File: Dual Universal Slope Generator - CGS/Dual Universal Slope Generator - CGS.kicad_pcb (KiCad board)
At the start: 2 copper layers, 115.3 x 110 mm, 146 parts, among them J1 CV_IN_A, J10 TRIG_IN_B, J11 IN_B, J12 1V/OCT_B, J13 DC_OUT_B, J14 AC_COUPLED_OUT_B, J15 END_OUT_B, J16 BIPOLAR_OUT_B, J17 CV_POT_A, J18 FALL_POT_A, J19 RISE_POT_A, J2 TRIG_IN_A, J20 SW_RISE_A, J21 SW_FALL_A, J22 CV_POT_2_B, J23 FALL_POT_B, J24 RISE_POT_B, J25 SW_RISE_B, J26 SW_FALL_B, J3 IN_A, J4 1V/OCT_A, J5 DC_OUT_A, J6 AC_COUPLED_OUT_A, J7 END_OUT_A, J8 BIPOLAR_OUT_A, J9 CV_IN_B, Q1 2N3904, Q10 2N3906, Q11 2N3904, Q2 2N3906, Q3 2N3906, Q4 2N3906, Q5 2N3904, Q7 2N3904, Q8 2N3906, Q9 2N3906, U1 LF353, U2 TL072, U3 LM3900, U4 LF353, U5 TL072, U6 LM3900

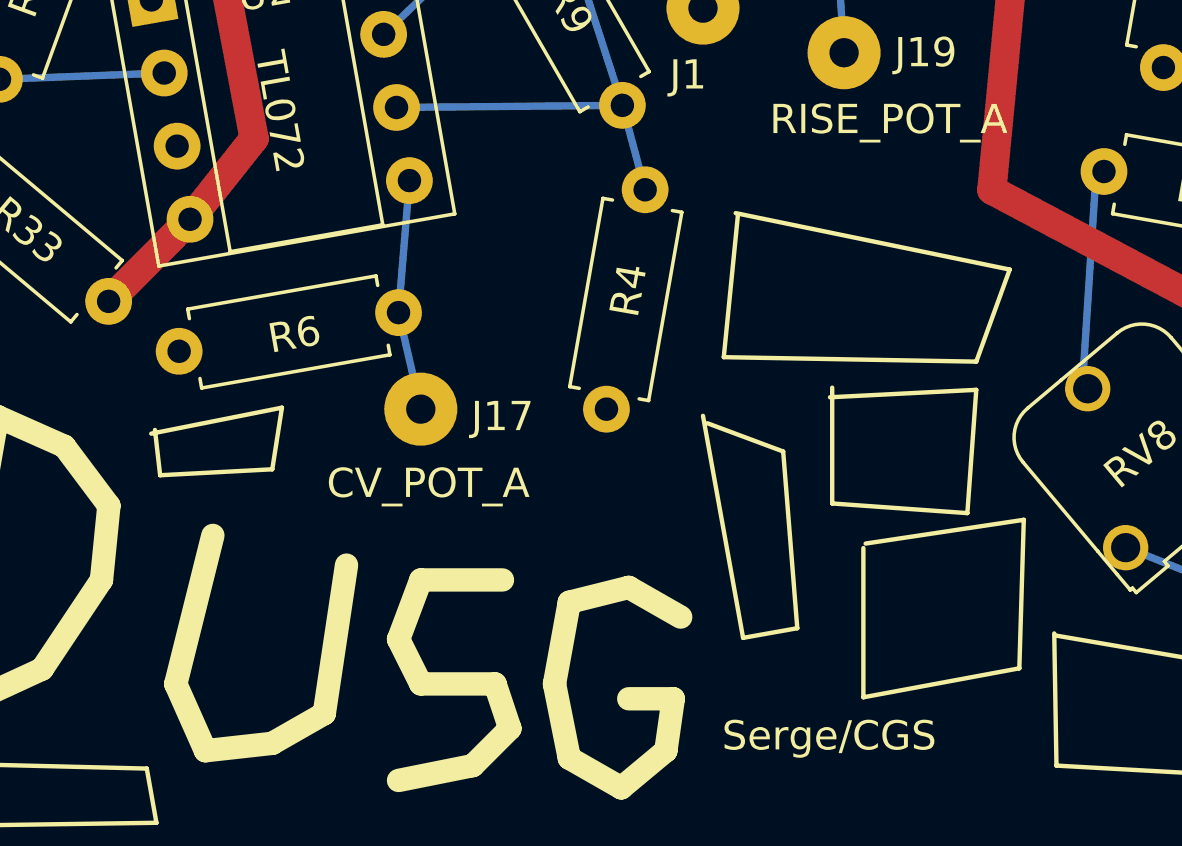
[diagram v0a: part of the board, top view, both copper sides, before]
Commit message: added power connectors to DUSG
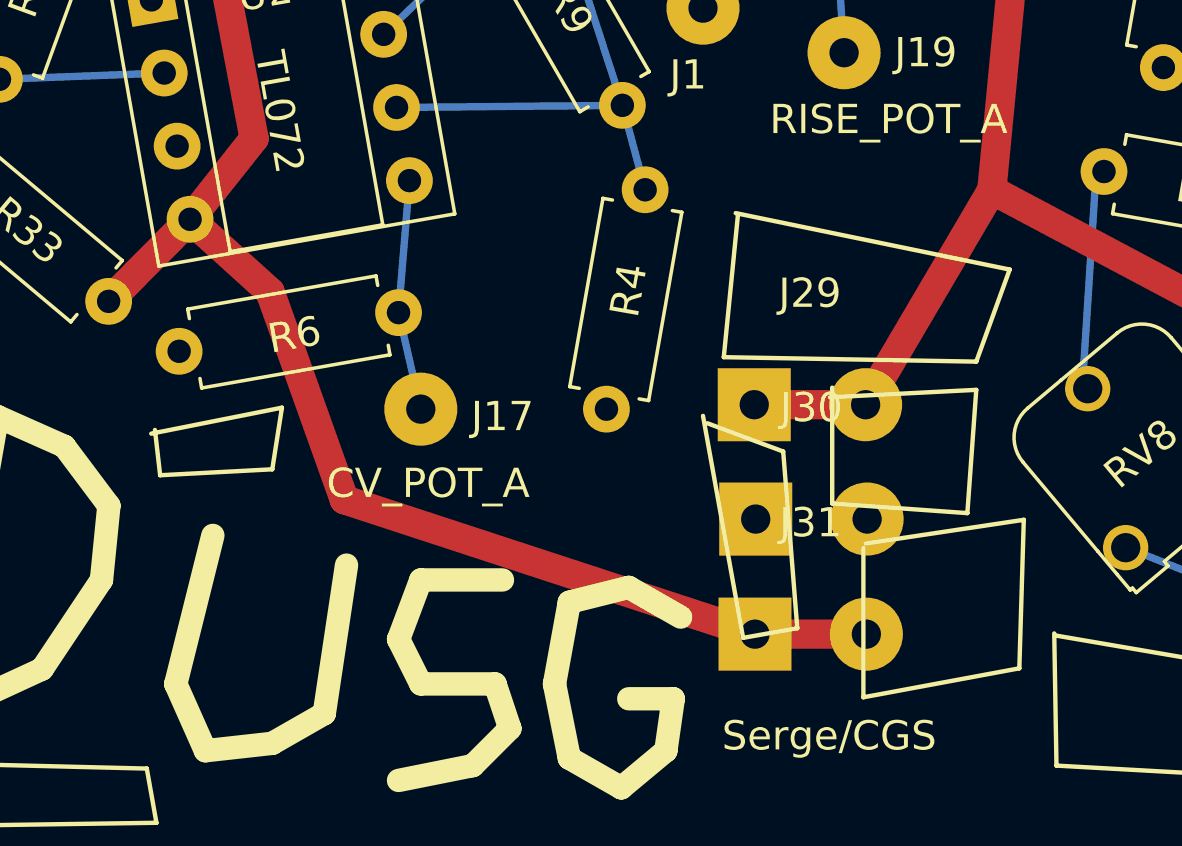
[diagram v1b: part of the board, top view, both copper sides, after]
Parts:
- added J29: +12V_Conn, Connector_Wire:SolderWirePad_1x02_P3.81mm_Drill1mm, F.Cu at (51.8, 106.5)
- added J30: GND_Conn, Connector_Wire:SolderWirePad_1x02_P3.81mm_Drill1mm, F.Cu at (51.8, 110.4)
- added J31: -12V_Conn, Connector_Wire:SolderWirePad_1x02_P3.81mm_Drill1mm, F.Cu at (51.8, 114.4)
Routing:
- net -12V: track 227.1 -> 256.9 mm
- net +12V: track 285.9 -> 298.2 mm
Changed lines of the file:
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@@
     (thickness 1.6)
     (drawings 1897)
-    (tracks 439)
+    (tracks 445)
     (zones 0)
-    (modules 146)
+    (modules 149)
     (nets 92)
   )
@@
     (44 Edge.Cuts user)
     (45 Margin user)
-    (46 B.CrtYd user hide)
-    (47 F.CrtYd user hide)
+    (46 B.CrtYd user)
+    (47 F.CrtYd user)
     (48 B.Fab user hide)
     (49 F.Fab user hide)
@@
     (add_net "Net-(U6-Pad5)")
   )
+  (module Connector_Wire:SolderWirePad_1x02_P3.81mm_Drill1mm (layer F.Cu)
+    (at 51.816 114.3762)
+    (descr "Wire solder connection")
+    (tags connector)
+    (attr virtual)
+    (fp_text reference J31 (at 1.905 -3.81) (layer F.SilkS)
+      (effects (font (size 1 1) (thickness 0.15)))
+    )
+    (fp_text value -12V_Conn (at 1.905 3.81) (layer F.Fab)
+      (effects (font (size 1 1) (thickness 0.15)))
+    )
+    (fp_line (start 5.56 1.75) (end -1.74 1.75) (layer F.CrtYd) (width 0.05))
+    (fp_line (start 5.56 1.75) (end 5.56 -1.75) (layer F.CrtYd) (width 0.05))
+    (fp_line (start -1.74 -1.75) (end -1.74 1.75) (layer F.CrtYd) (width 0.05))
+    (fp_line (start -1.74 -1.75) (end 5.56 -1.75) (layer F.CrtYd) (width 0.05))
+    (fp_text user %R (at 1.905 0) (layer F.Fab)
+      (effects (font (size 1 1) (thickness 0.15)))
+    )
+    (pad 2 thru_hole circle (at 3.81 0) (size 2.49936 2.49936) (drill 1.00076) (layers *.Cu *.Mask)
+      (net 70 -12V))
+    (pad 1 thru_hole rect (at 0 0) (size 2.49936 2.49936) (drill 1.00076) (layers *.Cu *.Mask)
+      (net 70 -12V))
+  )
+  (module Connector_Wire:SolderWirePad_1x02_P3.81mm_Drill1mm (layer F.Cu)
+    (at 51.8414 110.4392)
+    (descr "Wire solder connection")
+    (tags connector)
+    (attr virtual)
+    (fp_text reference J30 (at 1.905 -3.81) (layer F.SilkS)
+      (effects (font (size 1 1) (thickness 0.15)))
+    )
+    (fp_text value GND_Conn (at 1.905 3.81) (layer F.Fab)
+      (effects (font (size 1 1) (thickness 0.15)))
+    )
+    (fp_line (start 5.56 1.75) (end -1.74 1.75) (layer F.CrtYd) (width 0.05))
+    (fp_line (start 5.56 1.75) (end 5.56 -1.75) (layer F.CrtYd) (width 0.05))
+    (fp_line (start -1.74 -1.75) (end -1.74 1.75) (layer F.CrtYd) (width 0.05))
+    (fp_line (start -1.74 -1.75) (end 5.56 -1.75) (layer F.CrtYd) (width 0.05))
+    (fp_text user %R (at 1.905 0) (layer F.Fab)
+      (effects (font (size 1 1) (thickness 0.15)))
+    )
+    (pad 2 thru_hole circle (at 3.81 0) (size 2.49936 2.49936) (drill 1.00076) (layers *.Cu *.Mask)
+      (net 26 Earth))
+    (pad 1 thru_hole rect (at 0 0) (size 2.49936 2.49936) (drill 1.00076) (layers *.Cu *.Mask)
+      (net 26 Earth))
+  )
+  (module Connector_Wire:SolderWirePad_1x02_P3.81mm_Drill1mm (layer F.Cu)
+    (at 51.7906 106.5276)
+    (descr "Wire solder connection")
+    (tags connector)
+    (attr virtual)
+    (fp_text reference J29 (at 1.905 -3.81) (layer F.SilkS)
+      (effects (font (size 1 1) (thickness 0.15)))
+    )
+    (fp_text value +12V_Conn (at 1.905 3.81) (layer F.Fab)
+      (effects (font (size 1 1) (thickness 0.15)))
+    )
+    (fp_line (start 5.56 1.75) (end -1.74 1.75) (layer F.CrtYd) (width 0.05))
+    (fp_line (start 5.56 1.75) (end 5.56 -1.75) (layer F.CrtYd) (width 0.05))
+    (fp_line (start -1.74 -1.75) (end -1.74 1.75) (layer F.CrtYd) (width 0.05))
+    (fp_line (start -1.74 -1.75) (end 5.56 -1.75) (layer F.CrtYd) (width 0.05))
+    (fp_text user %R (at 1.905 0) (layer F.Fab)
+      (effects (font (size 1 1) (thickness 0.15)))
+    )
+    (pad 2 thru_hole circle (at 3.81 0) (size 2.49936 2.49936) (drill 1.00076) (layers *.Cu *.Mask)
+      (net 58 +12V))
+    (pad 1 thru_hole rect (at 0 0) (size 2.49936 2.49936) (drill 1.00076) (layers *.Cu *.Mask)
+      (net 58 +12V))
+  )
   (module Capacitor_THT:CP_Radial_D5.0mm_P2.00mm (layer F.Cu)
     (at 17.272 59.436 270)
@@
   (segment (start 45.72 86.868) (end 55.88 87.122) (width 1) (layer F.Cu) (net 58))
   (segment (start 55.88 87.122) (end 60.84321 89.547462) (width 1) (layer F.Cu) (net 58))
+  (segment (start 51.7906 106.5276) (end 55.6006 106.5276) (width 1) (layer F.Cu) (net 58))
+  (segment (start 55.6006 106.5276) (end 59.917581 99.185145) (width 1) (layer F.Cu) (net 58))
   (segment (start 54.586502 70.531615) (end 54.101329 67.780062) (width 0.25) (layer B.Cu) (net 59))
   (segment (start 41.91 71.886886) (end 38.862 73.406) (width 0.25) (layer B.Cu) (net 59))
@@
   (segment (start 99.695397 66.420603) (end 98.717074 65.697074) (width 0.5) (layer B.Cu) (net 70))
   (segment (start 105.984193 71.071542) (end 99.695397 66.420603) (width 1) (layer B.Cu) (net 70))
+  (segment (start 55.626 114.3762) (end 51.816 114.3762) (width 1) (layer F.Cu) (net 70))
+  (segment (start 51.816 114.3762) (end 37.7698 109.7788) (width 1) (layer F.Cu) (net 70))
+  (segment (start 37.7698 109.7788) (end 35.2298 102.6668) (width 1) (layer F.Cu) (net 70))
+  (segment (start 35.2298 102.6668) (end 32.492716 100.185919) (width 1) (layer F.Cu) (net 70))
   (segment (start 55.649519 27.527567) (end 59.096636 28.312055) (width 0.25) (layer B.Cu) (net 71))
   (segment (start 66.716636 28.312055) (end 65.889191 20.856827) (width 0.25) (layer B.Cu) (net 72))

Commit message: DUSG updates
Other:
- rule via_min_size: 0.4 -> 0.6
